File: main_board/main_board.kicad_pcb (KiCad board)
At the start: 4 copper layers, 85 x 55 mm, 47 parts, among them J1 USB_B_Micro, J2 Conn_ARM_JTAG_SWD_10, Q1 NX3008PBK,215, Q2 T2N7002AK,LM, U1 SSD1306, U2 ESP32-S2-SOLO, U3 TLV62568PDRLT, U4 MCP73832, Y1 SC32S-7PF20PPM

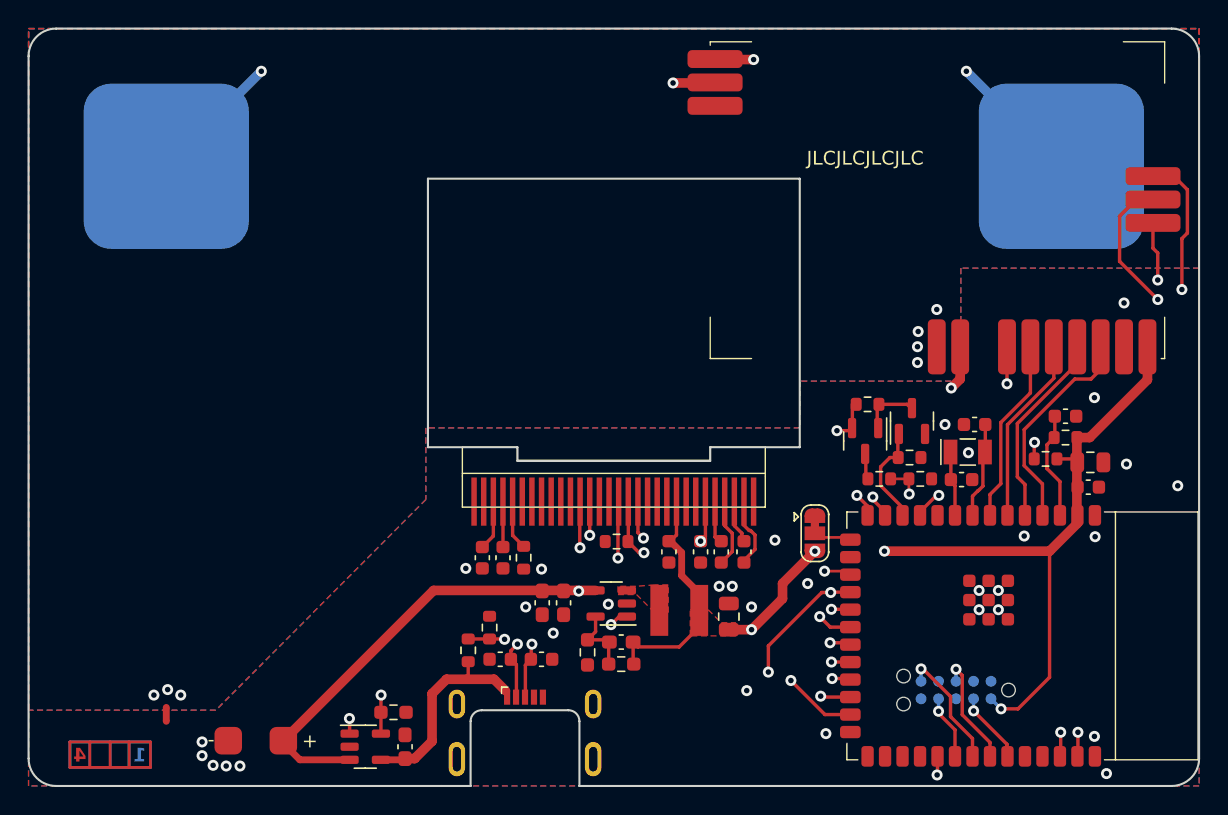
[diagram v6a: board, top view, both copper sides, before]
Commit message: Place battery terminals directly onto PCB
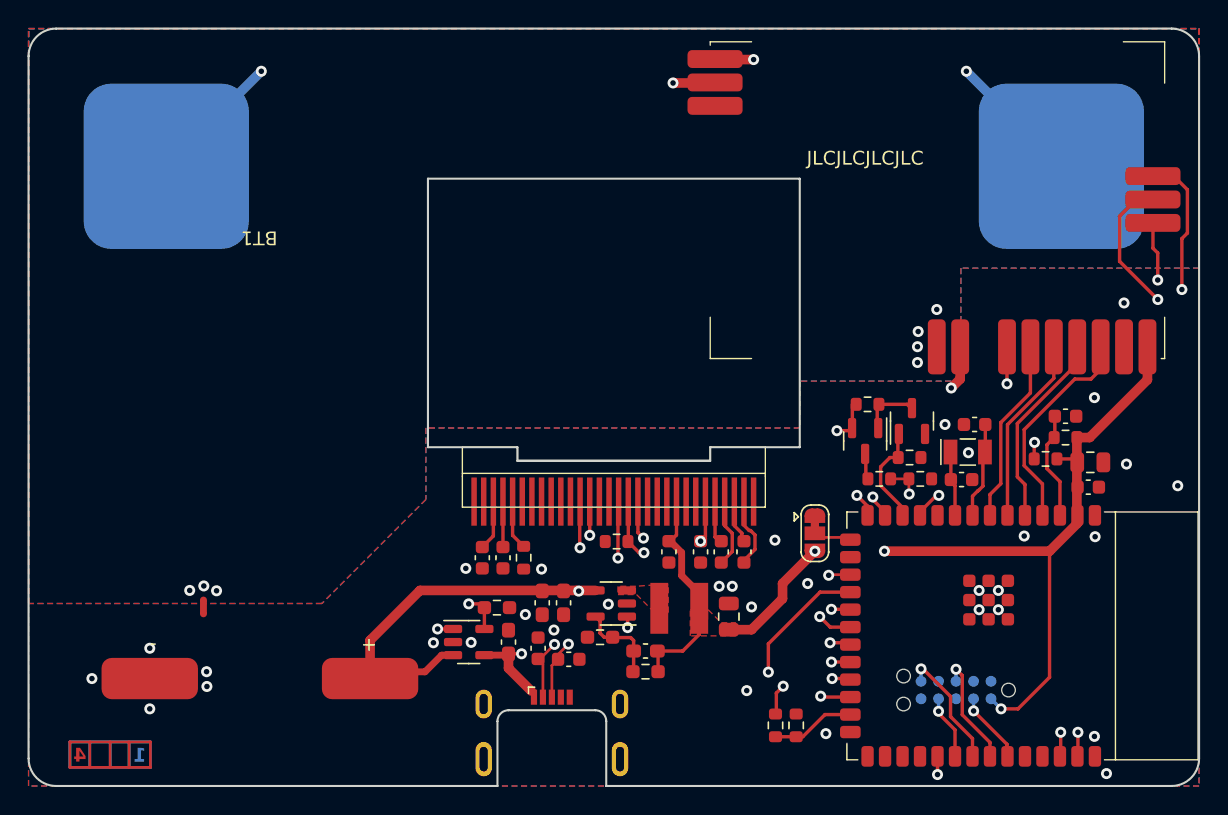
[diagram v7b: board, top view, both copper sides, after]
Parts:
- BT1: footprint main_board_parts:Battery -> main_board_parts:Battery_transplant
- moved R10 23.4 mm to (135.7, 95.6)
- moved R5 23.0 mm to (134.2, 95.6), turned to -90 degrees
- moved R6 10.7 mm to (114.0, 87.0)
- moved U4 10.7 mm to (112.0, 89.5)
- moved C14 10.7 mm to (114.8, 89.5)
- moved NT1 8.25 mm to (92.7, 87.0)
- moved C10 2.86 mm to (117.0, 90.0), turned to 90 degrees
- moved C11 1.97 mm to (119.2, 90.8)
- moved J1 1.95 mm to (118.0, 93.0)
- moved C17 1.88 mm to (124.8, 90.2)
- moved R7 1.85 mm to (124.8, 91.7)
- moved R8 1.43 mm to (121.5, 89.2), turned to 180 degrees
- moved BT1 0.57 mm to (96.8, 47.2)
- moved L1 0.15 mm to (127.2, 87.1)
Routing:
- net /VBUS_DETECT: track 30.4 -> 6.10 mm, vias 2 -> 0
- net +5V: track 15.5 -> 29.3 mm, vias 0 -> 2
- net /CHG_STAT: track 39.5 -> 33.1 mm
- net +BATT: track 82.4 -> 77.4 mm
- net /CHG_CURRENT: track 41.3 -> 36.6 mm, vias 3 -> 2
- net /USB_D+: track 33.9 -> 31.6 mm
- net /USB_D-: track 36.7 -> 34.4 mm
- net +3V3: track 78.8 -> 77.3 mm, vias 4 -> 3
- net Net-(U3-FB): track 4.91 -> 6.28 mm
- net /BATT_ADC: track 15.6 -> 14.8 mm
- net GND: vias 31 -> 33
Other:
- outline, holes or cut-outs redrawn

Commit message: Close #15: add battery protection components
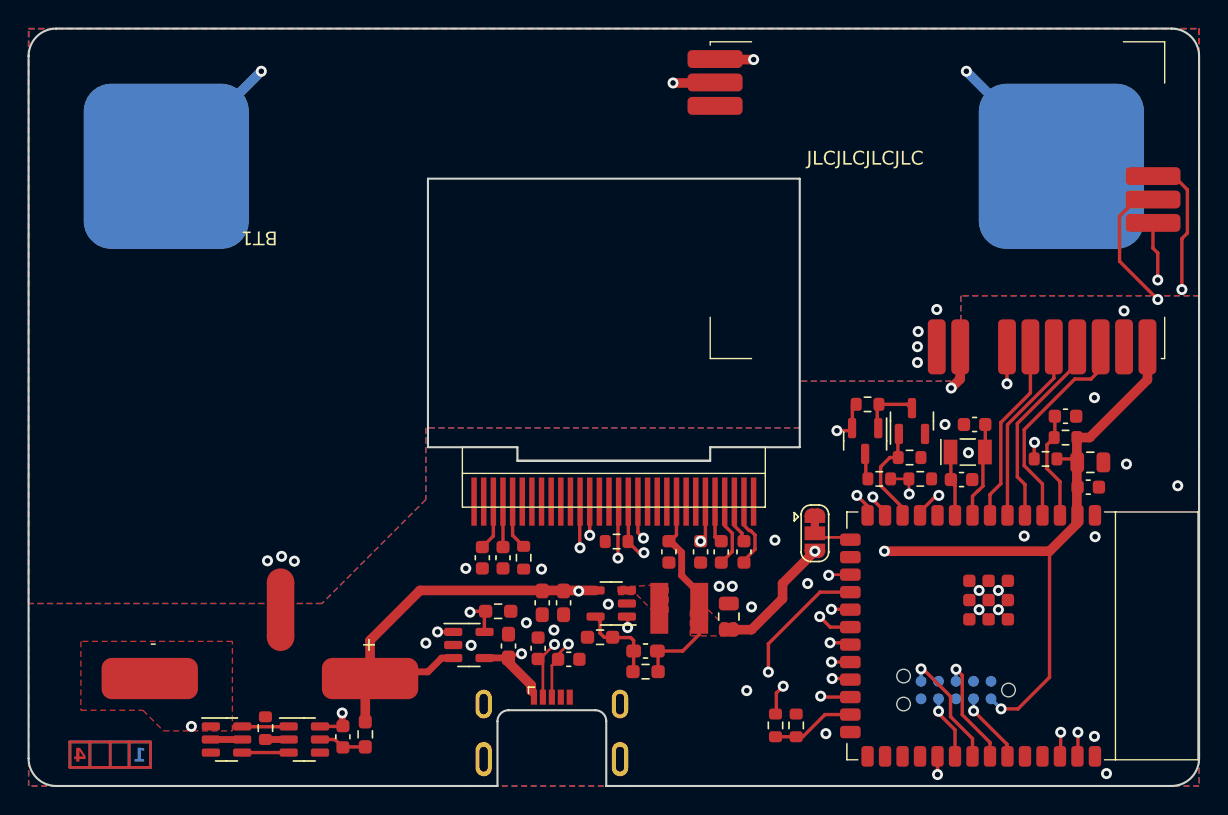
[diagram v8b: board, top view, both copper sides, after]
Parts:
- added C19: 1uF, Capacitor_SMD:C_0603_1608Metric_Pad1.08x0.95mm_HandSolder, F.Cu at (114.8, 89.8)
- added R14: 5k, Resistor_SMD:R_0603_1608Metric_Pad0.98x0.95mm_HandSolder, F.Cu at (114.1, 87.3)
- added R15: 1k, Resistor_SMD:R_0603_1608Metric, F.Cu at (97.2, 95.8)
- added U5: ~, Package_TO_SOT_SMD:SOT-23-6, F.Cu at (100.0, 96.6)
- added U6: ~, Package_TO_SOT_SMD:SOT-23-6, F.Cu at (94.4, 96.6)
- C14: value 1uF -> 100nF; footprint Capacitor_SMD:C_0603_1608Metric_Pad1.08x0.95mm_HandSolder -> Capacitor_SMD:C_0603_1608Metric
- NT1: footprint NetTie:NetTie-2_SMD_Pad0.5mm -> NetTie:NetTie-2_SMD_Pad2.0mm
- R6: value 5k -> 100
- moved C14 13.9 mm to (102.8, 96.4)
- moved R6 13.3 mm to (104.5, 96.2), turned to -90 degrees
- moved NT1 5.60 mm to (98.3, 87.2)
- moved U4 0.21 mm to (112.0, 89.8)
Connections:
- BT1 pad 2: GND -> Net-(BT1--)
- C14 pad 1: +5V -> Net-(U5-VCC)
- C14 pad 2: GND -> Net-(BT1--)
- R6 pad 1: GND -> +BATT
- R6 pad 2: /CHG_CURRENT -> Net-(U5-VCC)
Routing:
- net Net-(BT1--): track 0.00 -> 14.0 mm, vias 0 -> 2
- net Net-(U5-VCC): track 0.00 -> 3.54 mm
- net Net-(U5-OD): track 0.00 -> 3.40 mm
- net Net-(U5-OC): track 0.00 -> 3.38 mm
- net +BATT: track 77.4 -> 80.6 mm
- net Net-(U6-D-Pad2): track 0.00 -> 2.28 mm
- net Net-(U5-VM): track 0.00 -> 1.69 mm
- net /CHG_CURRENT: track 36.6 -> 35.8 mm
- net +5V: track 29.3 -> 28.6 mm
- net GND: vias 33 -> 28
- added copper zone on F.Cu, net Net-(BT1--)
